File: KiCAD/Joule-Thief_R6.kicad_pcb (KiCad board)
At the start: 2 copper layers, 95 x 60 mm, 35 parts, among them J2 Conn_01x06_Socket, Q1 AO3400A, Q2 AO3400A, SW1 SW_SPST, SW2 SW_SPST, U1 INA219AxD, U2 LTC3105xMS, U3 AD5280, U4 INA219AxD, U5 DW01A

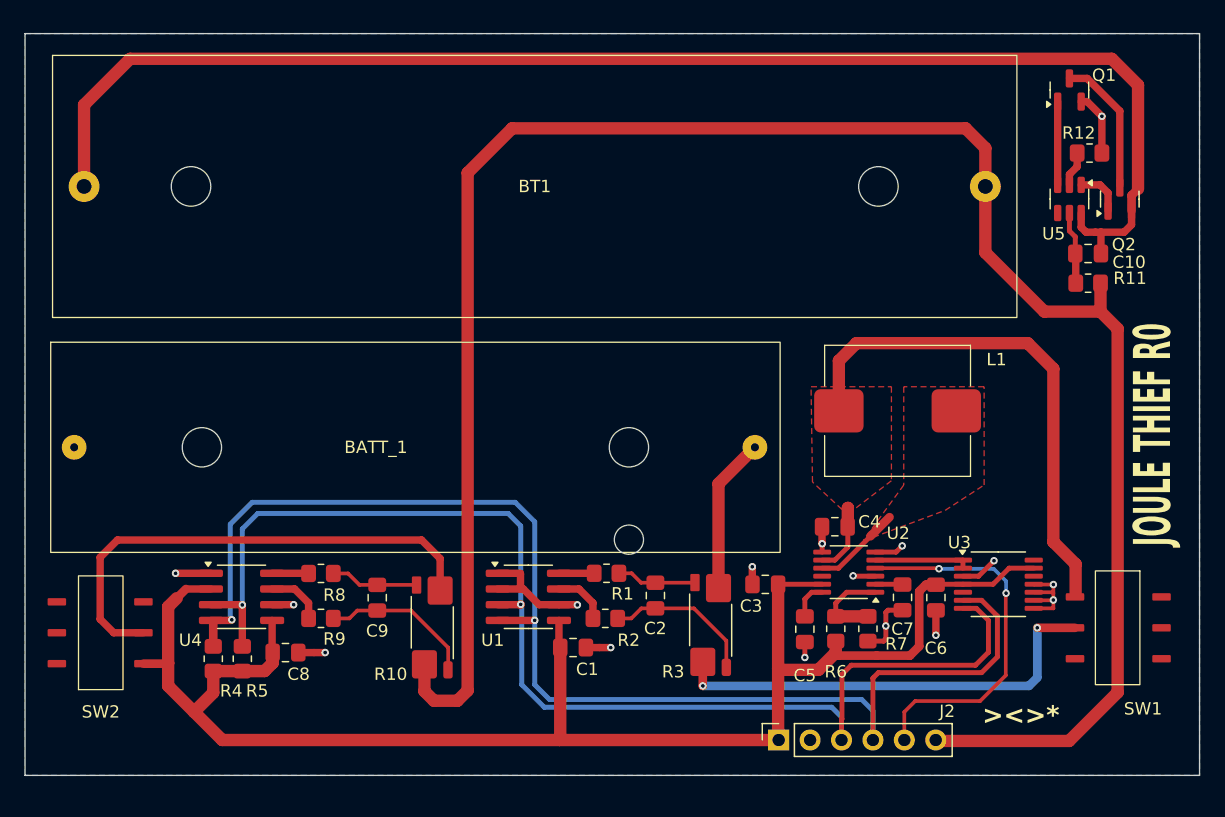
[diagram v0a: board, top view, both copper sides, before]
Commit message: board ordered
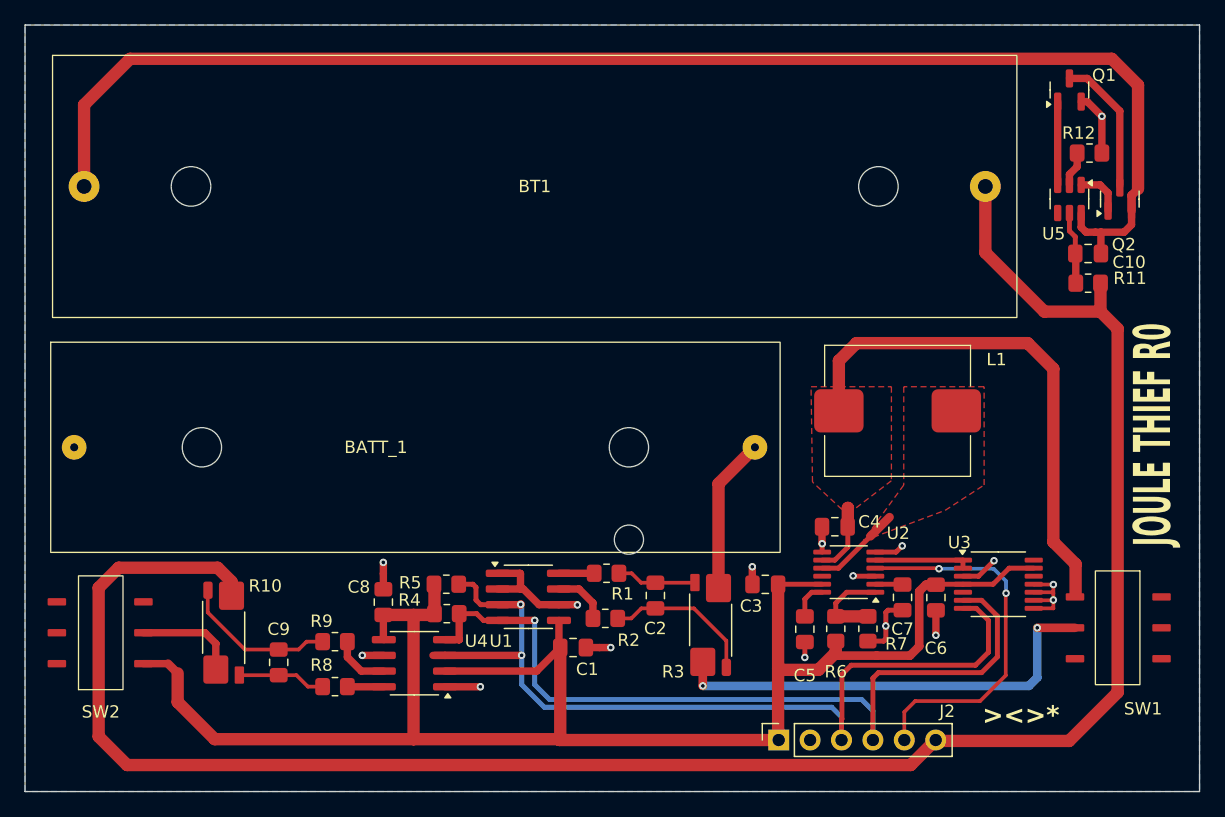
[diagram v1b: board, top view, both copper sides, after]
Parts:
- moved R4 19.2 mm to (92.7, 77.0), turned to 0 degrees
- moved R5 17.6 mm to (92.7, 74.6), turned to 0 degrees
- moved R10 16.9 mm to (74.7, 78.5), turned to 90 degrees
- moved U4 15.0 mm to (90.1, 81.0), turned to 180 degrees
- moved C9 9.53 mm to (79.1, 80.9), turned to -90 degrees
- moved R8 9.23 mm to (83.7, 82.9), turned to 180 degrees
- moved C8 8.91 mm to (87.6, 76.0), turned to 90 degrees
- moved R9 2.20 mm to (83.7, 79.2), turned to 180 degrees
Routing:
- net SCL: track 106.7 -> 67.9 mm, vias 2 -> 1
- net Net-(SW2-B): track 40.2 -> 8.32 mm
- net SDA: track 102.1 -> 71.8 mm
- net V5+: track 129.1 -> 137.6 mm
- net LITH: track 162.0 -> 161.2 mm
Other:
- board size 95 x 60 mm -> 95 x 62 mm
